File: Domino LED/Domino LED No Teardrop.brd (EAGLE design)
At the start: 27.9 x 10.2 mm, 23 parts, among them J1 MH11-1

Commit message: Changed copyright
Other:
- board text added: "Reference designs are provided "AS IS" and "WITH ALL FAULTS". The Domino Team disclaims all other warranties express or implied, regarding this product, including but not limited to, any implied warranties of merchantibility or fitness for any particular application."
- board text added: "The Domino Team may make changes to specifications and product descriptions at any time, without notice."
- board text added: "© 2014, The Domino Team. All rights reserved."
- board text removed: "Michel Stempin may make changes to specifications and product descriptions at any time, without notice."
- board text removed: "Reference designs are provided "AS IS" and "WITH ALL FAULTS". Michel Stempin disclaims all other warranties express or implied, regarding this product, including but not limited to, any implied warranties of merchantibility or fitness for any particular application."
- board text removed: "© 2014, Michel Stempin. All rights reserved."
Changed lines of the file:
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@@
 See creativecommons.org/licenses/by-sa/4.0/</text>
 <text x="34.29" y="-51.943" size="0.8128" layer="48" ratio="20">Reference designs are provided "AS IS" and "WITH ALL FAULTS".
-Michel Stempin disclaims all other warranties express or implied,
+The Domino Team disclaims all other warranties express or implied,
 regarding this product, including but not limited to, any implied warranties of
 merchantibility or fitness for any particular application.</text>
-<text x="34.29" y="-55.753" size="0.8128" layer="48" ratio="20">Michel Stempin may make changes to specifications and product descriptions
+<text x="34.29" y="-55.753" size="0.8128" layer="48" ratio="20">The Domino Team may make changes to specifications and product descriptions
 at any time, without notice.</text>
-<text x="74.93" y="-41.91" size="1.27" layer="48" ratio="20">© 2014, Michel Stempin.
+<text x="74.93" y="-41.91" size="1.27" layer="48" ratio="20">© 2014, The Domino Team.
 All rights reserved.</text>
 <text x="115.57" y="-57.15" size="1.778" layer="48">Rev.</text>

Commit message: ... and all the files I missed
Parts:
- removed U$4: (no value), Domino:DOMINO_LOGO_SMALL
- moved J1 5.08 mm to (1.27, 6.35)
- moved D1 3.81 mm to (3.81, 3.17)
- moved D2 3.81 mm to (6.35, 3.17)
- moved D3 3.81 mm to (8.89, 3.17)
- moved D4 3.81 mm to (11.4, 3.17)
- moved D5 3.81 mm to (14.0, 3.17)
- moved D6 3.81 mm to (16.5, 3.17)
- moved D7 3.81 mm to (19.1, 3.17)
- moved D8 3.81 mm to (21.6, 3.17)
- moved D9 3.81 mm to (24.1, 3.17)
- moved DRILEGEND 1.27 mm to (81.5, 59.9)
- flipped R1 to the bottom, turned to 270 degrees
- flipped R2 to the bottom, turned to 270 degrees
- flipped R3 to the bottom, turned to 270 degrees
- flipped R4 to the bottom, turned to 270 degrees
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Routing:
- net +3V3: track 25.5 -> 29.9 mm, vias 1 -> 0
- net N$9: track 1.78 -> 2.03 mm, vias 0 -> 1
- net N$8: track 1.78 -> 2.03 mm, vias 0 -> 1
- net N$7: track 1.78 -> 2.03 mm, vias 0 -> 1
- net N$6: track 1.78 -> 2.03 mm, vias 0 -> 1
- net N$5: track 1.78 -> 2.03 mm, vias 0 -> 1
- net N$4: track 1.78 -> 2.03 mm, vias 0 -> 1
- net N$3: track 1.78 -> 2.03 mm, vias 0 -> 1
- net N$2: track 1.78 -> 2.03 mm, vias 0 -> 1
- net N$10: track 1.78 -> 2.03 mm, vias 0 -> 1
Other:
- board size 27.9 x 10.2 mm -> 27.9 x 7.6 mm
- board text removed: "ELD3"
- board text removed: "Rev. A"

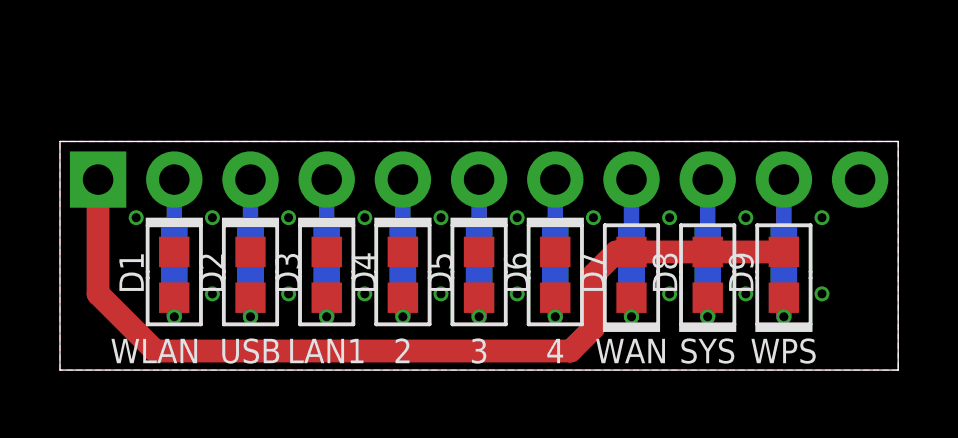
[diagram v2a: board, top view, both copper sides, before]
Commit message: Made Single Ethernet tile with component on top side only
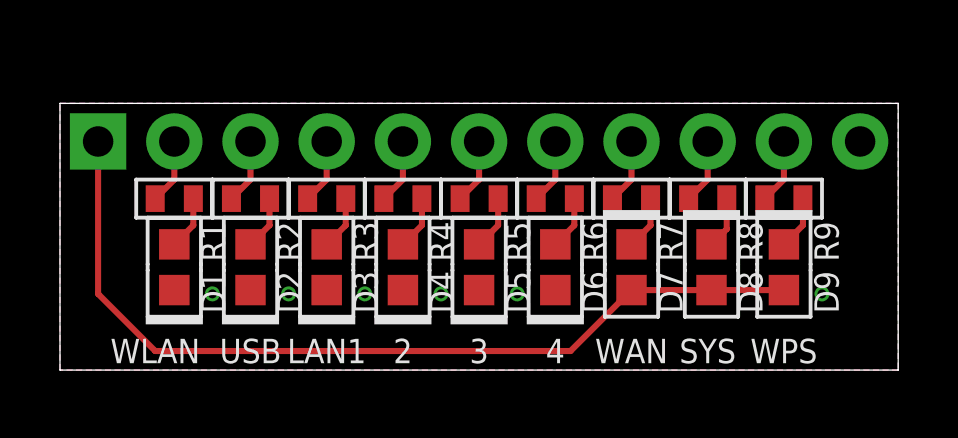
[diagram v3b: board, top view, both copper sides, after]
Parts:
- moved R1 1.90 mm to (3.81, 5.71), flipped to the top, turned to 0 degrees
- moved R2 1.90 mm to (6.35, 5.71), flipped to the top, turned to 0 degrees
- moved R3 1.90 mm to (8.89, 5.71), flipped to the top, turned to 0 degrees
- moved R4 1.90 mm to (11.4, 5.71), flipped to the top, turned to 0 degrees
- moved R5 1.90 mm to (14.0, 5.71), flipped to the top, turned to 0 degrees
- moved R6 1.90 mm to (16.5, 5.71), flipped to the top, turned to 0 degrees
- moved R7 1.90 mm to (19.1, 5.71), flipped to the top, turned to 0 degrees
- moved R8 1.90 mm to (21.6, 5.71), flipped to the top, turned to 0 degrees
- moved R9 1.90 mm to (24.1, 5.71), flipped to the top, turned to 0 degrees
- moved J1 1.27 mm to (1.27, 7.62)
- moved D8 0.28 mm to (21.7, 3.43), turned to 270 degrees
- moved D1 0.25 mm to (3.81, 3.43), turned to 90 degrees
- moved D2 0.25 mm to (6.35, 3.43), turned to 90 degrees
- moved D3 0.25 mm to (8.89, 3.43), turned to 90 degrees
- moved D4 0.25 mm to (11.4, 3.43), turned to 90 degrees
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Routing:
- net N$8: track 2.03 -> 1.73 mm, vias 1 -> 0
- net N$7: track 2.03 -> 1.79 mm, vias 1 -> 0
- net N$10: track 2.03 -> 1.79 mm, vias 1 -> 0
- net N$6: track 2.03 -> 1.79 mm, vias 1 -> 0
- net N$5: track 2.03 -> 1.79 mm, vias 1 -> 0
- net N$4: track 2.03 -> 1.79 mm, vias 1 -> 0
- net N$2: track 2.03 -> 1.79 mm, vias 1 -> 0
- net N$3: track 2.03 -> 1.79 mm, vias 1 -> 0
- net N$9: track 2.03 -> 1.79 mm, vias 1 -> 0
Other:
- board size 27.9 x 7.6 mm -> 27.9 x 8.9 mm

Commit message: Domino LED Rev. C: changed Logos
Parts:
- added U$4: DOMINO_LOGO, Domino:DOMINO_LOGO
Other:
- board text removed: "Domino Core"
- board text removed: "Domino Pi"
- board text removed: "Domino Qi"
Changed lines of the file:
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@@
 <layer number="54" name="bGND_GNDA" color="1" fill="9" visible="no" active="no"/>
 <layer number="56" name="wert" color="7" fill="1" visible="no" active="no"/>
+<layer number="90" name="Modules" color="5" fill="1" visible="yes" active="yes"/>
 <layer number="91" name="Nets" color="2" fill="1" visible="no" active="no"/>
 <layer number="92" name="Busses" color="1" fill="1" visible="no" active="no"/>
@@
 <layer number="145" name="DrillLegend_01-16" color="2" fill="9" visible="yes" active="yes"/>
 <layer number="146" name="DrillLegend_01-20" color="3" fill="9" visible="no" active="yes"/>
+<layer number="147" name="mMeasures" color="7" fill="1" visible="no" active="no"/>
 <layer number="148" name="mDocument" color="7" fill="1" visible="no" active="no"/>
 <layer number="149" name="mReference" color="7" fill="1" visible="no" active="no"/>
@@
 <text x="115.57" y="-57.15" size="1.778" layer="48">Rev.</text>
 <text x="121.92" y="-57.15" size="1.778" layer="48">&gt;REV</text>
-<wire x1="-34.970125" y1="-47.888025" x2="-32.27605" y2="-45.193946875" width="0.1016" layer="48"/>
-<wire x1="-32.27605" y1="-45.193946875" x2="-29.581971875" y2="-42.499871875" width="0.1016" layer="48"/>
-<wire x1="-29.581971875" y1="-42.499871875" x2="-27.785921875" y2="-42.499871875" width="0.1016" layer="48" curve="-90"/>
-<wire x1="-27.785921875" y1="-42.499871875" x2="-25.989871875" y2="-44.295921875" width="0.1016" layer="48"/>
-<wire x1="-25.989871875" y1="-44.295921875" x2="-25.989871875" y2="-46.091971875" width="0.1016" layer="48" curve="-90"/>
-<wire x1="-25.989871875" y1="-46.091971875" x2="-28.683946875" y2="-48.78605" width="0.1016" layer="48"/>
-<wire x1="-28.683946875" y1="-48.78605" x2="-31.378025" y2="-51.480125" width="0.1016" layer="48"/>
-<wire x1="-31.378025" y1="-51.480125" x2="-33.174075" y2="-51.480125" width="0.1016" layer="48" curve="-90"/>
-<wire x1="-33.174075" y1="-51.480125" x2="-34.970125" y2="-49.684075" width="0.1016" layer="48"/>
-<wire x1="-34.970125" y1="-49.684075" x2="-34.970125" y2="-47.888025" width="0.1016" layer="48" curve="-90"/>
-<wire x1="-32.27605" y1="-45.193946875" x2="-28.683946875" y2="-48.78605" width="0.1016" layer="48"/>
-<circle x="-34.0721" y="-48.78605" radius="0.635" width="0" layer="48"/>
-<circle x="-32.27605" y="-46.989996875" radius="0.635" width="0" layer="48"/>
-<circle x="-32.27605" y="-50.5821" radius="0.635" width="0" layer="48"/>
-<circle x="-30.48" y="-48.78605" radius="0.635" width="0" layer="48"/>
-<circle x="-28.683946875" y="-46.99" radius="0.635" width="0" layer="48"/>
-<circle x="-28.683946875" y="-43.397896875" radius="0.635" width="0" layer="48"/>
-<text x="-30.48" y="-53.975" size="1.778" layer="48" rot="R45" align="center-left">Domino
-Pi</text>
-<wire x1="-48.940125" y1="-47.888025" x2="-46.24605" y2="-45.193946875" width="0.1016" layer="48"/>
-<wire x1="-46.24605" y1="-45.193946875" x2="-43.551971875" y2="-42.499871875" width="0.1016" layer="48"/>
-<wire x1="-43.551971875" y1="-42.499871875" x2="-41.755921875" y2="-42.499871875" width="0.1016" layer="48" curve="-90"/>
-<wire x1="-41.755921875" y1="-42.499871875" x2="-39.959871875" y2="-44.295921875" width="0.1016" layer="48"/>
-<wire x1="-39.959871875" y1="-44.295921875" x2="-39.959871875" y2="-46.091971875" width="0.1016" layer="48" curve="-90"/>
-<wire x1="-39.959871875" y1="-46.091971875" x2="-42.653946875" y2="-48.78605" width="0.1016" layer="48"/>
-<wire x1="-42.653946875" y1="-48.78605" x2="-45.348025" y2="-51.480125" width="0.1016" layer="48"/>
-<wire x1="-45.348025" y1="-51.480125" x2="-47.144075" y2="-51.480125" width="0.1016" layer="48" curve="-90"/>
-<wire x1="-47.144075" y1="-51.480125" x2="-48.940125" y2="-49.684075" width="0.1016" layer="48"/>
-<wire x1="-48.940125" y1="-49.684075" x2="-48.940125" y2="-47.888025" width="0.1016" layer="48" curve="-90"/>
-<wire x1="-46.24605" y1="-45.193946875" x2="-42.653946875" y2="-48.78605" width="0.1016" layer="48"/>
-<circle x="-48.0421" y="-48.78605" radius="0.635" width="0" layer="48"/>
-<circle x="-46.24605" y="-46.989996875" radius="0.635" width="0" layer="48"/>
-<circle x="-46.24605" y="-50.5821" radius="0.635" width="0" layer="48"/>
-<circle x="-44.45" y="-48.78605" radius="0.635" width="0" layer="48"/>
-<circle x="-42.653946875" y="-46.99" radius="0.635" width="0" layer="48"/>
-<circle x="-42.653946875" y="-43.397896875" radius="0.635" width="0" layer="48"/>
-<text x="-44.45" y="-53.975" size="1.778" layer="48" rot="R45" align="center-left">Domino
-Core</text>
-<wire x1="-21.000125" y1="-47.888025" x2="-18.30605" y2="-45.193946875" width="0.1016" layer="48"/>
-<wire x1="-18.30605" y1="-45.193946875" x2="-15.611971875" y2="-42.499871875" width="0.1016" layer="48"/>
-<wire x1="-15.611971875" y1="-42.499871875" x2="-13.815921875" y2="-42.499871875" width="0.1016" layer="48" curve="-90"/>
-<wire x1="-13.815921875" y1="-42.499871875" x2="-12.019871875" y2="-44.295921875" width="0.1016" layer="48"/>
-<wire x1="-12.019871875" y1="-44.295921875" x2="-12.019871875" y2="-46.091971875" width="0.1016" layer="48" curve="-90"/>
-<wire x1="-12.019871875" y1="-46.091971875" x2="-14.713946875" y2="-48.78605" width="0.1016" layer="48"/>
-<wire x1="-14.713946875" y1="-48.78605" x2="-17.408025" y2="-51.480125" width="0.1016" layer="48"/>
-<wire x1="-17.408025" y1="-51.480125" x2="-19.204075" y2="-51.480125" width="0.1016" layer="48" curve="-90"/>
-<wire x1="-19.204075" y1="-51.480125" x2="-21.000125" y2="-49.684075" width="0.1016" layer="48"/>
-<wire x1="-21.000125" y1="-49.684075" x2="-21.000125" y2="-47.888025" width="0.1016" layer="48" curve="-90"/>
-<wire x1="-18.30605" y1="-45.193946875" x2="-14.713946875" y2="-48.78605" width="0.1016" layer="48"/>
-<circle x="-20.1021" y="-48.78605" radius="0.635" width="0" layer="48"/>
-<circle x="-18.30605" y="-46.989996875" radius="0.635" width="0" layer="48"/>
-<circle x="-18.30605" y="-50.5821" radius="0.635" width="0" layer="48"/>
-<circle x="-16.51" y="-48.78605" radius="0.635" width="0" layer="48"/>
-<circle x="-14.713946875" y="-46.99" radius="0.635" width="0" layer="48"/>
-<circle x="-14.713946875" y="-43.397896875" radius="0.635" width="0" layer="48"/>
-<text x="-16.51" y="-53.975" size="1.778" layer="48" rot="R45" align="center-left">Domino
-Qi</text>
 <text x="6.35" y="4.445" size="0.8128" layer="22" rot="MR90" align="center">LED1</text>
 <text x="8.89" y="4.445" size="0.8128" layer="22" rot="MR90" align="center">LED2</text>
@@
 </plain>
 <attributes>
-<attribute name="DATE" value="20140810"/>
+<attribute name="DATE" value="20141230"/>
 <attribute name="DRAWN" value="M.STEMPIN"/>
-<attribute name="REV" value="B"/>
+<attribute name="REV" value="C"/>
 </attributes>
 <variantdefs>
@@
 </element>
 <element name="DRILEGEND" library="drilegend" package="DRILEGEND" value="" x="81.534" y="59.944"/>
+<element name="U$4" library="Domino" package="DOMINO_LOGO" value="DOMINO_LOGO" x="-45.72" y="-48.26">
+<attribute name="BOM" value="EXCLUDE" x="-45.72" y="-48.26" size="1.778" layer="27" display="off"/>
+</element>
 </elements>
 <signals>

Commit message: Domino LED Rev. D: changed silkscreen font ratio to 20%
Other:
- board text added: "© 2014-2015, The Domino Team. All rights reserved."
- board text removed: "© 2014, The Domino Team. All rights reserved."
